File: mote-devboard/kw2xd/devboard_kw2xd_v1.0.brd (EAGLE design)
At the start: 100 x 80 mm, 11 parts, among them Q3 RED

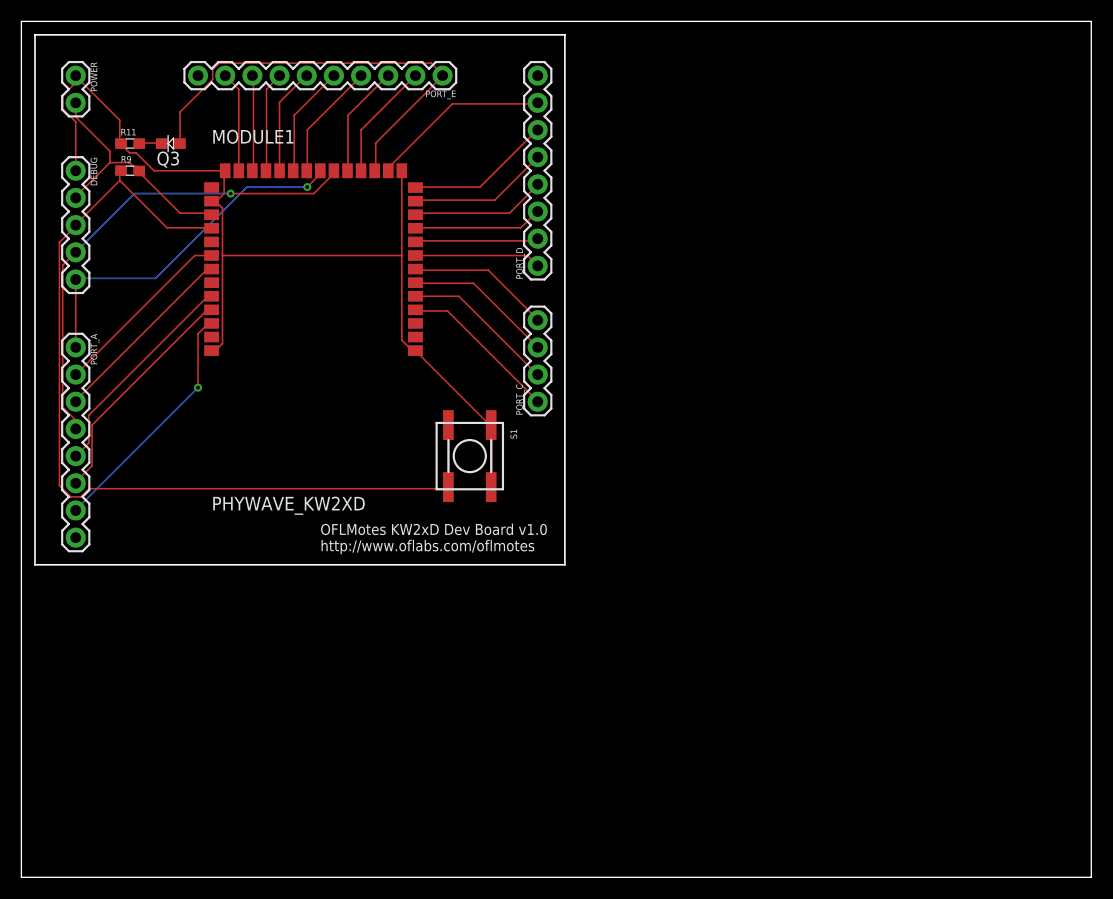
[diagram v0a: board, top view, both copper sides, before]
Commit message: -Increased clearances from 6 to 8mil to fit Eurocircuits PCB Manufacturer's requirements - Order a first batch of 2 naked prototype boards
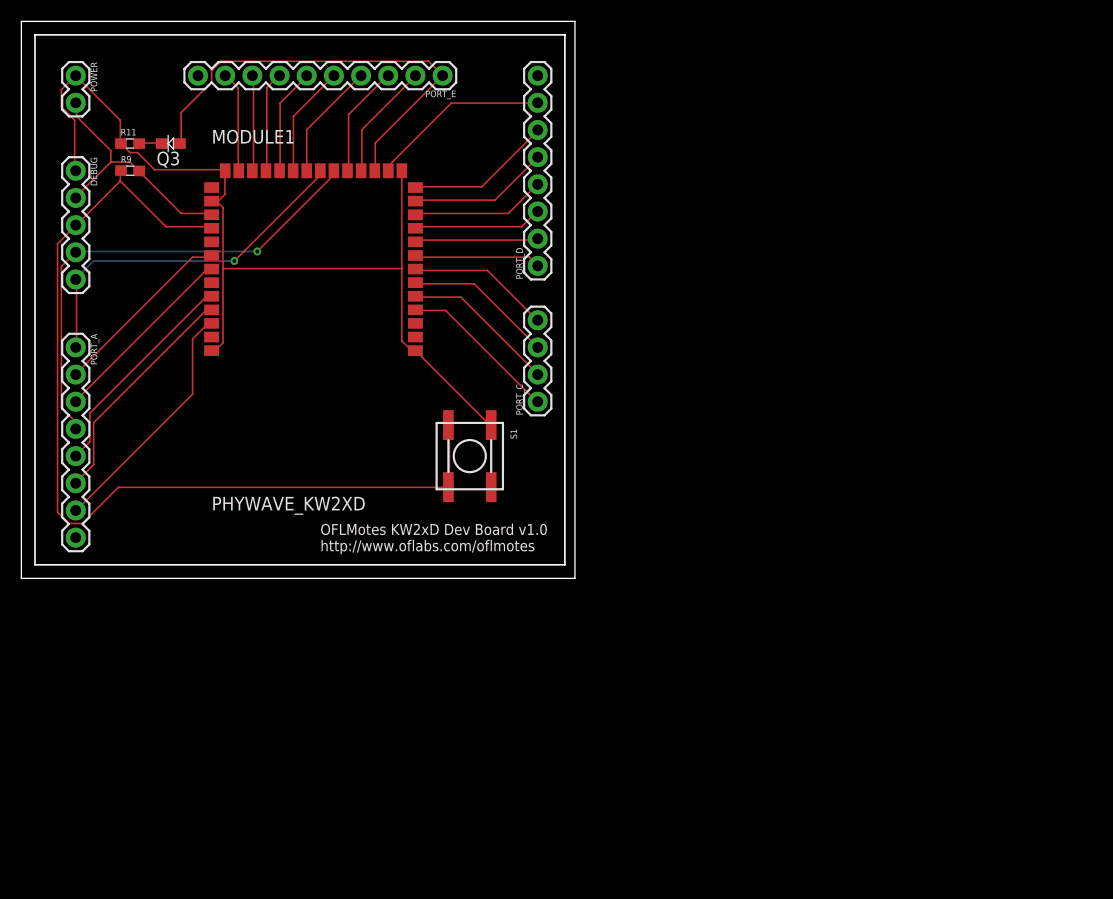
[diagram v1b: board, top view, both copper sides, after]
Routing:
- net NRST: track 85.4 -> 89.1 mm
- net PTA19: track 22.9 -> 23.0 mm, vias 1 -> 0
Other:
- board size 100 x 80 mm -> 51.7 x 52.1 mm
